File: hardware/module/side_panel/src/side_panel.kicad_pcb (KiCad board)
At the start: 2 copper layers, 96 x 120.2 mm, 35 parts, among them J1 Top Connector, J2 Bottom Connecor, J3 Conn_01x05, J4 Conn_01x09, M1 GA12-N20 12V 60rpm, Q1 AP2302B, U1 ITR8307, U2 ITR8307, U3 ITR8307, U4 PY32F003F1xPx, U5 L9110S, U6 74LVC1G66, U7 NUP4202

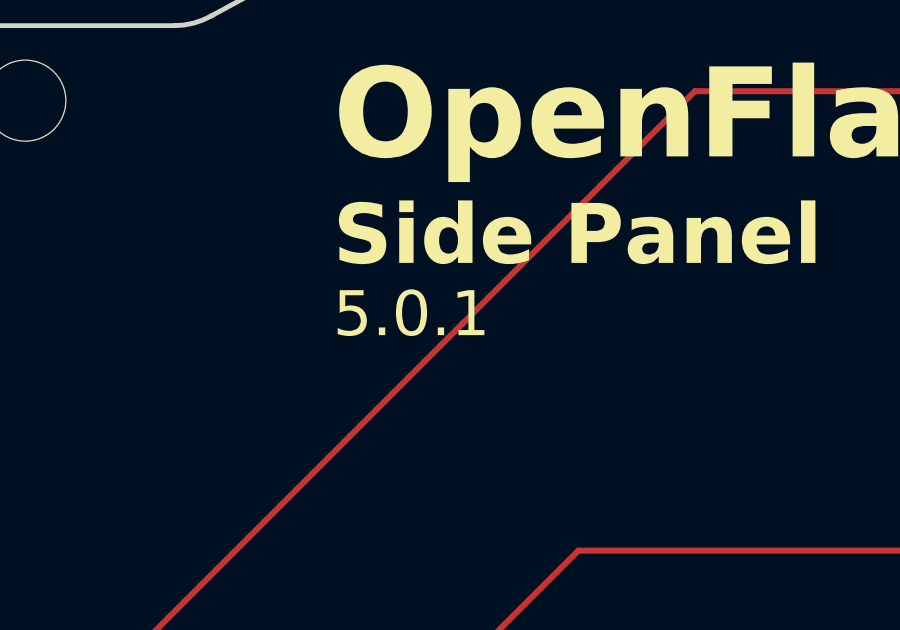
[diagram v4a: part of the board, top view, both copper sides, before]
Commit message: Change sidepanel IR resistor to 15ohm and finalize encoder wheel design
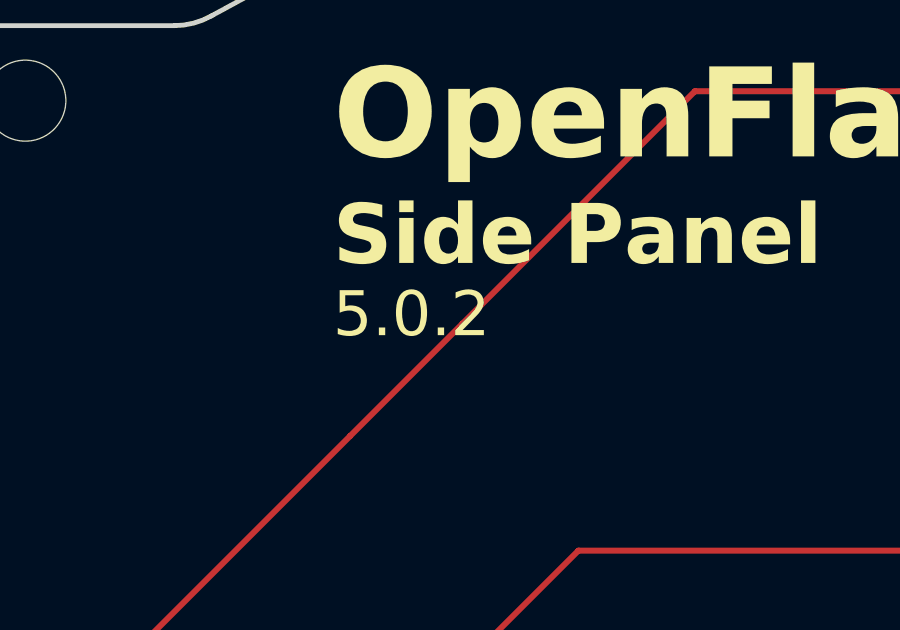
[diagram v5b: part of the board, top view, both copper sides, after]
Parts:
- R4: value 20R -> 15R
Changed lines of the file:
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@@
 		(title "Side Panel")
 		(date "${DATE}")
-		(rev "5.0.1")
+		(rev "5.0.2")
 		(company "OpenFlap")
 		(comment 1 "${GIT_TAG}")
@@
 			)
 		)
-		(property "Value" "20R"
+		(property "Value" "15R"
 			(at 0 1.65 90)
 			(layer "F.Fab")
@@
 			(justify left bottom mirror)
 		)
-		(render_cache "5.0.1" 0
+		(render_cache "5.0.2" 0
 			(polygon
 				(pts
@@
 			(polygon
 				(pts
-					(xy 97.065369 96.427204) (xy 97.065369 96.294213) (xy 96.692043 96.294213) (xy 96.692043 95.11452)
-					(xy 97.065369 95.279384) (xy 97.065369 95.139799) (xy 96.634891 94.950023) (xy 96.540002 94.950023)
-					(xy 96.540002 96.294213) (xy 96.113554 96.294213) (xy 96.113554 96.427204)
+					(xy 97.086618 96.427204) (xy 97.086618 96.315462) (xy 96.495672 95.669562) (xy 96.444194 95.610907)
+					(xy 96.397418 95.550591) (xy 96.387228 95.535839) (xy 96.348943 95.469377) (xy 96.332274 95.427029)
+					(xy 96.317728 95.354394) (xy 96.316154 95.319318) (xy 96.328467 95.240973) (xy 96.365407 95.173551)
+					(xy 96.403715 95.13467) (xy 96.469541 95.093162) (xy 96.546623 95.068884) (xy 96.626464 95.061764)
+					(xy 96.70189 95.067431) (xy 96.773193 95.084433) (xy 96.818439 95.102064) (xy 96.887922 95.14036)
+					(xy 96.95039 95.185025) (xy 97.01016 95.235135) (xy 97.017009 95.241282) (xy 97.105669 95.135769)
+					(xy 97.047485 95.086379) (xy 96.981756 95.038861) (xy 96.915736 94.999864) (xy 96.871562 94.978599)
+					(xy 96.796565 94.951358) (xy 96.719492 94.934206) (xy 96.640345 94.927144) (xy 96.624266 94.926942)
+					(xy 96.544045 94.931772) (xy 96.46962 94.946262) (xy 96.394447 94.973358) (xy 96.387961 94.976401)
+					(xy 96.32217 95.01482) (xy 96.262347 95.066804) (xy 96.225662 95.112688) (xy 96.189495 95.18109)
+					(xy 96.17002 95.256601) (xy 96.166311 95.310892) (xy 96.171687 95.386214) (xy 96.185362 95.447179)
+					(xy 96.213979 95.515446) (xy 96.253139 95.579803) (xy 96.299446 95.64197) (xy 96.349584 95.70194)
+					(xy 96.392357 95.749796) (xy 96.896475 96.296411) (xy 96.134803 96.294213) (xy 96.134803 96.427204)
 				)
 			)
@@
 			(justify left bottom)
 		)
-		(render_cache "5.0.1" 0
+		(render_cache "5.0.2" 0
 			(polygon
 				(pts
@@
 			(polygon
 				(pts
-					(xy 78.91563 96.427204) (xy 78.91563 96.294213) (xy 79.288956 96.294213) (xy 79.288956 95.11452)
-					(xy 78.91563 95.279384) (xy 78.91563 95.139799) (xy 79.346108 94.950023) (xy 79.440997 94.950023)
-					(xy 79.440997 96.294213) (xy 79.867445 96.294213) (xy 79.867445 96.427204)
+					(xy 78.894381 96.427204) (xy 78.894381 96.315462) (xy 79.485327 95.669562) (xy 79.536805 95.610907)
+					(xy 79.583581 95.550591) (xy 79.593771 95.535839) (xy 79.632056 95.469377) (xy 79.648725 95.427029)
+					(xy 79.663271 95.354394) (xy 79.664845 95.319318) (xy 79.652532 95.240973) (xy 79.615592 95.173551)
+					(xy 79.577284 95.13467) (xy 79.511458 95.093162) (xy 79.434376 95.068884) (xy 79.354535 95.061764)
+					(xy 79.279109 95.067431) (xy 79.207806 95.084433) (xy 79.16256 95.102064) (xy 79.093077 95.14036)
+					(xy 79.030609 95.185025) (xy 78.970839 95.235135) (xy 78.96399 95.241282) (xy 78.87533 95.135769)
+					(xy 78.933514 95.086379) (xy 78.999243 95.038861) (xy 79.065263 94.999864) (xy 79.109437 94.978599)
+					(xy 79.184434 94.951358) (xy 79.261507 94.934206) (xy 79.340654 94.927144) (xy 79.356733 94.926942)
+					(xy 79.436954 94.931772) (xy 79.511379 94.946262) (xy 79.586552 94.973358) (xy 79.593038 94.976401)
+					(xy 79.658829 95.01482) (xy 79.718652 95.066804) (xy 79.755337 95.112688) (xy 79.791504 95.18109)
+					(xy 79.810979 95.256601) (xy 79.814688 95.310892) (xy 79.809312 95.386214) (xy 79.795637 95.447179)
+					(xy 79.76702 95.515446) (xy 79.72786 95.579803) (xy 79.681553 95.64197) (xy 79.631415 95.70194)
+					(xy 79.588642 95.749796) (xy 79.084524 96.296411) (xy 79.846196 96.294213) (xy 79.846196 96.427204)
 				)
 			)

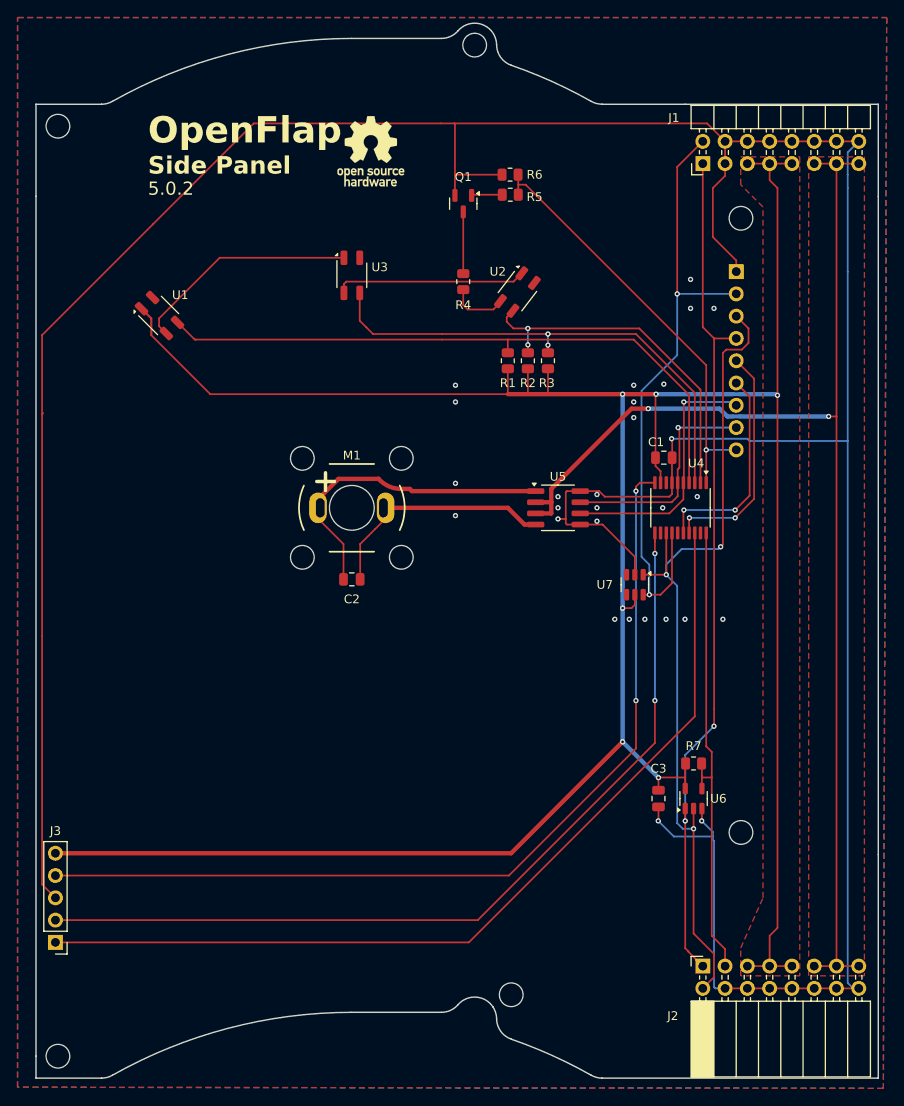
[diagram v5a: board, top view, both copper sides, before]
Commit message: Change CAD design to work with 35mm stepper motor
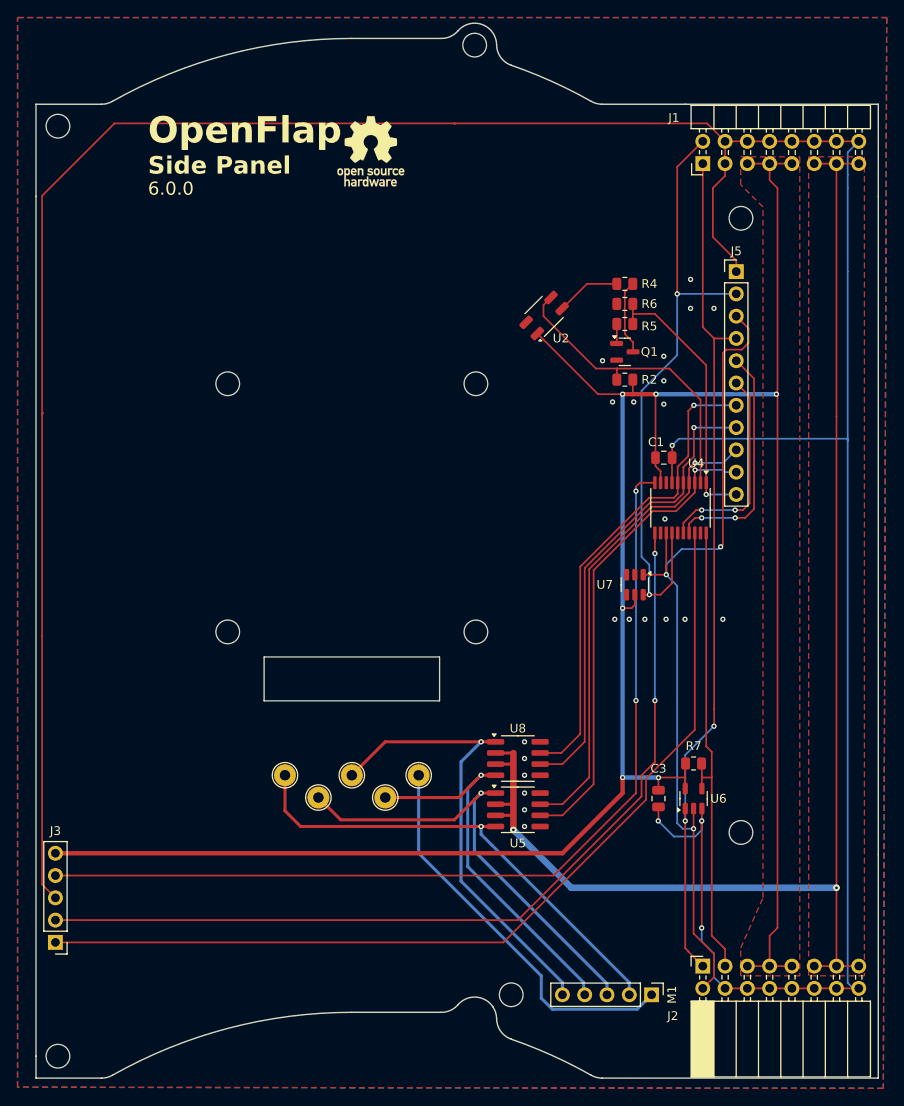
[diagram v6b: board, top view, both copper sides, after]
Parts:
- removed C2: 100nF, Capacitor_SMD:C_0805_2012Metric
- removed J4: Conn_01x09, Connector_PinHeader_2.54mm:PinHeader_1x09_P2.54mm_Vertical
- removed R1, R3: 20K, Resistor_SMD:R_0805_2012Metric
- removed U1, U3: ITR8307, OptoDevice:OnSemi_CASE100CY
- added J5: Conn_01x11, Connector_PinHeader_2.54mm:PinHeader_1x11_P2.54mm_Vertical, F.Cu at (140.8, 105.3)
- added TP1: TestPoint, TestPoint:TestPoint_THTPad_D2.5mm_Drill1.2mm, F.Cu at (93.1, 165.2)
- added TP2: TestPoint, TestPoint:TestPoint_THTPad_D2.5mm_Drill1.2mm, F.Cu at (89.3, 162.7)
- added TP3: TestPoint, TestPoint:TestPoint_THTPad_D2.5mm_Drill1.2mm, F.Cu at (96.9, 162.7)
- added TP4: TestPoint, TestPoint:TestPoint_THTPad_D2.5mm_Drill1.2mm, F.Cu at (100.8, 165.2)
- added TP5: TestPoint, TestPoint:TestPoint_THTPad_D2.5mm_Drill1.2mm, F.Cu at (104.6, 162.7)
- added U8: L9110S, Package_SO:SOP-8_3.76x4.96mm_P1.27mm, F.Cu at (115.9, 160.8)
- M1: value GA12-N20 12V 60rpm -> ~; footprint GA12-N20:GA12-N20 Motor Vertical -> Connector_PinHeader_2.54mm:PinHeader_1x05_P2.54mm_Vertical
- R4: value 15R -> 47R
- moved M1 65.2 mm to (131.1, 187.7), turned to -90 degrees
- moved U5 34.7 mm to (115.9, 166.6)
- moved Q1 25.0 mm to (128.1, 114.4), turned to 0 degrees
- moved R6 19.7 mm to (128.1, 108.9)
- moved R5 19.7 mm to (128.1, 111.2)
- moved R4 18.4 mm to (128.1, 106.7), turned to 0 degrees
- moved H9 12.0 mm to (82.8, 146.3)
- moved H10 12.0 mm to (82.8, 118.0)
- moved H7 12.0 mm to (111.1, 146.3)
- moved H8 12.0 mm to (111.1, 118.0)
- moved R2 11.3 mm to (128.1, 117.6), turned to 180 degrees
- moved U2 4.05 mm to (118.9, 110.3), turned to 135 degrees
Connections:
- net Net-(M1--) renamed /Motor O2
- M1 pad 1: Net-(M1-+) -> /Motor C
- R2 pad 2: /IR Sens B -> /IR Sens A
- U2 pad 1: Net-(U2-A) -> +5V
- U2 pad 3: /IR Sens B -> /IR Sens A
- U4 pad 2: /IR Sens B -> /IR Sens A
- U4 pad 3: /IR Sens Z -> /Motor A1
- U4 pad 4: /IR Sens A -> /Motor A2
- U4 pad 5: /Motor IN_A -> /Motor A3
- U4 pad 6: /Motor IN_B -> /Motor A4
- U5 pad 1: Net-(M1-+) -> /Motor O1
- U5 pad 6: /Motor IN_A -> /Motor A1
- U5 pad 7: /Motor IN_B -> /Motor A2
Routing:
- net /IR Sens Z: track 57.1 -> 0.00 mm, vias 2 -> 0
- net /Motor A4: track 0.00 -> 55.3 mm, vias 0 -> 1
- net /Motor A2: track 0.00 -> 54.6 mm, vias 0 -> 1
- net /Motor A1: track 0.00 -> 54.5 mm, vias 0 -> 1
- net /Motor A3: track 0.00 -> 53.5 mm, vias 0 -> 1
- net +5V: track 324.7 -> 271.7 mm
- net /Motor O3: track 0.00 -> 52.5 mm, vias 0 -> 1
- net /Motor O1: track 0.00 -> 52.1 mm, vias 0 -> 1
- net /Motor C: track 0.00 -> 45.0 mm
- net /Motor O4: track 0.00 -> 44.8 mm, vias 0 -> 1
- net /IR Sens B: track 40.2 -> 0.00 mm, vias 2 -> 0
- net /IR Sens A: track 73.2 -> 35.1 mm
- net GND: track 397.8 -> 362.9 mm, vias 28 -> 26
- net Net-(M1-+): track 34.7 -> 0.00 mm
- net /Motor IN_A: track 29.7 -> 0.00 mm, vias 1 -> 0
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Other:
- outline, holes or cut-outs redrawn
- board text added: "A1"
- board text added: "A2"
- board text added: "A3"
- board text added: "A4"
- board text added: "C"
- board text added: "MOT A1"
- board text added: "MOT A2"
- board text added: "MOT A3"
- board text added: "MOT A4"
- board text removed: "MOT A"
- board text removed: "MOT B"

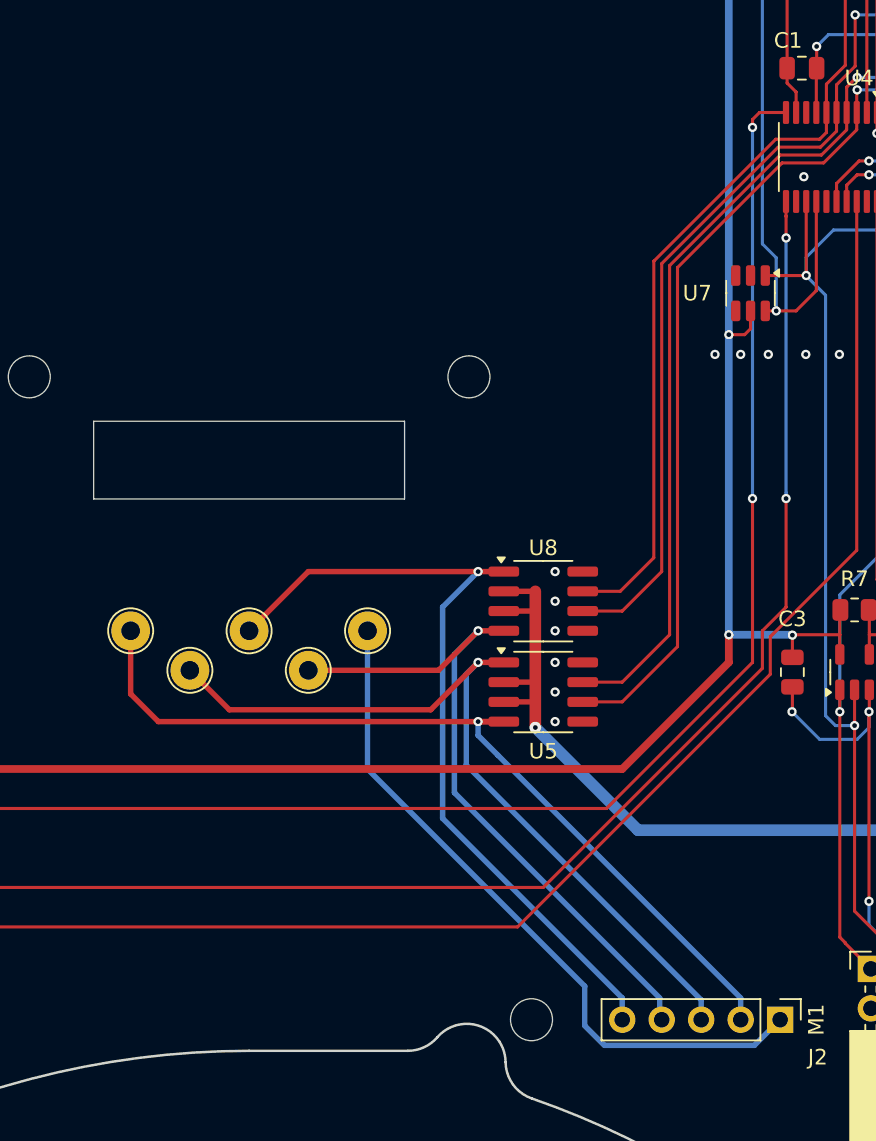
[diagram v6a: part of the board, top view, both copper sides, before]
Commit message: Create proper stepper driver.
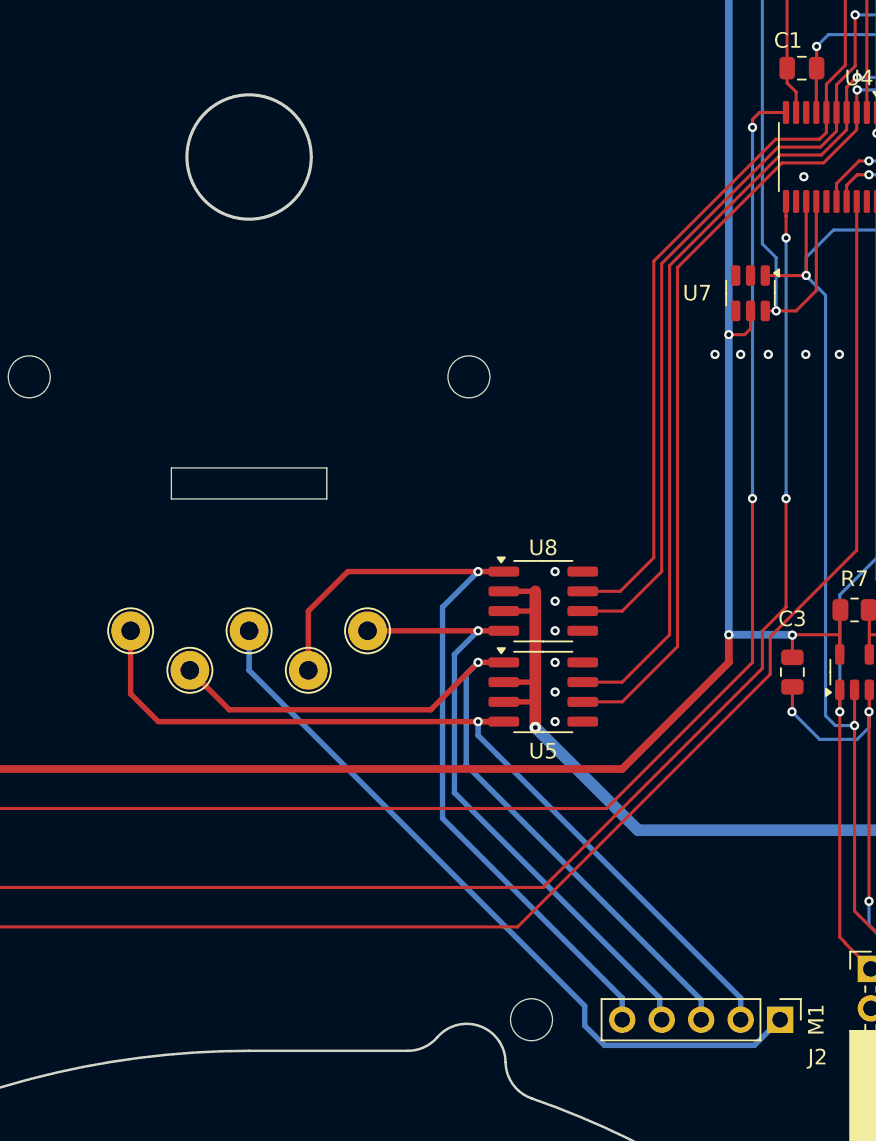
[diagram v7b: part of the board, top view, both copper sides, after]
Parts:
- moved TP5 7.62 mm to (96.9, 162.7)
- moved TP3 4.58 mm to (100.8, 165.2)
- moved TP4 4.58 mm to (104.6, 162.7)
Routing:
- net /Motor O4: track 44.8 -> 39.9 mm
- net /Motor C: track 45.0 -> 48.1 mm
- net /Motor O3: track 52.5 -> 52.0 mm
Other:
- outline, holes or cut-outs redrawn
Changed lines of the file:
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@@
 	(footprint "TestPoint:TestPoint_THTPad_D2.5mm_Drill1.2mm"
 		(layer "F.Cu")
-		(at 104.564 162.662204 90)
+		(at 96.944 162.662204 90)
 		(descr "THT pad as test Point, diameter 2.5mm, hole diameter 1.2mm ")
 		(tags "test point THT pad")
@@
 	(footprint "TestPoint:TestPoint_THTPad_D2.5mm_Drill1.2mm"
 		(layer "F.Cu")
-		(at 100.754 165.202204 90)
+		(at 104.564 162.662204 90)
 		(descr "THT pad as test Point, diameter 2.5mm, hole diameter 1.2mm ")
 		(tags "test point THT pad")
@@
 	(footprint "TestPoint:TestPoint_THTPad_D2.5mm_Drill1.2mm"
 		(layer "F.Cu")
-		(at 96.944 162.662204 90)
+		(at 100.754 165.202204 90)
 		(descr "THT pad as test Point, diameter 2.5mm, hole diameter 1.2mm ")
 		(tags "test point THT pad")
@@
 	)
 	(gr_line
-		(start 106.944 149.182204)
-		(end 106.944 154.182204)
+		(start 101.944 152.182204)
+		(end 101.944 154.182204)
 		(stroke
 			(width 0.05)
@@
 	)
 	(gr_line
-		(start 86.944 149.182204)
-		(end 106.944 149.182204)
+		(start 91.944 154.182204)
+		(end 101.944 154.182204)
 		(stroke
 			(width 0.05)
@@
 		(layer "Edge.Cuts")
 	)
+	(gr_circle
+		(center 96.944 132.182204)
+		(end 100.944 132.182204)
+		(stroke
+			(width 0.2)
+			(type default)
+		)
+		(fill none)
+		(layer "Edge.Cuts")
+	)
 	(gr_line
 		(start 156.947732 197.182204)
@@
 	)
 	(gr_line
-		(start 106.944 154.182204)
-		(end 86.944 154.182204)
+		(start 91.944 152.182204)
+		(end 101.944 152.182204)
 		(stroke
 			(width 0.05)
@@
 	)
 	(gr_line
-		(start 86.944 154.182204)
-		(end 86.944 149.182204)
+		(start 91.944 154.182204)
+		(end 91.944 152.182204)
 		(stroke
 			(width 0.05)
@@
 	(segment
 		(start 111.676 162.662204)
-		(end 109.136 165.202204)
-		(width 0.35)
-		(layer "F.Cu")
-		(net 25)
-	)
-	(segment
-		(start 109.136 165.202204)
-		(end 100.754 165.202204)
+		(end 104.564 162.662204)
 		(width 0.35)
 		(layer "F.Cu")
@@
 	)
 	(segment
-		(start 113.3295 158.852204)
-		(end 111.676 158.852204)
+		(start 100.754 161.392204)
+		(end 100.754 165.202204)
 		(width 0.35)
 		(layer "F.Cu")
@@
 	)
 	(segment
-		(start 111.676 158.852204)
-		(end 100.754 158.852204)
+		(start 103.294 158.852204)
+		(end 100.754 161.392204)
 		(width 0.35)
 		(layer "F.Cu")
@@
 	)
 	(segment
-		(start 100.754 158.852204)
-		(end 96.944 162.662204)
+		(start 113.3295 158.852204)
+		(end 111.676 158.852204)
+		(width 0.35)
+		(layer "F.Cu")
+		(net 27)
+	)
+	(segment
+		(start 111.676 158.852204)
+		(end 103.294 158.852204)
 		(width 0.35)
 		(layer "F.Cu")
@@
 	)
 	(segment
-		(start 129.456 189.332204)
-		(end 131.107 187.681204)
+		(start 119.804 189.332204)
+		(end 118.534 188.062204)
 		(width 0.35)
 		(layer "B.Cu")
@@
 	)
 	(segment
-		(start 104.564 171.552204)
-		(end 118.534 185.522204)
+		(start 96.944 165.202204)
+		(end 96.944 162.662204)
 		(width 0.35)
 		(layer "B.Cu")
@@
 	)
 	(segment
-		(start 104.564 162.662204)
-		(end 104.564 171.552204)
+		(start 131.107 187.681204)
+		(end 129.456 189.332204)
 		(width 0.35)
 		(layer "B.Cu")
@@
 	)
 	(segment
-		(start 118.534 188.062204)
-		(end 119.804 189.332204)
+		(start 118.534 186.792204)
+		(end 96.944 165.202204)
 		(width 0.35)
 		(layer "B.Cu")
@@
 	)
 	(segment
-		(start 118.534 185.522204)
-		(end 118.534 188.062204)
+		(start 129.456 189.332204)
+		(end 119.804 189.332204)
 		(width 0.35)
 		(layer "B.Cu")
@@
 	)
 	(segment
-		(start 119.804 189.332204)
-		(end 129.456 189.332204)
+		(start 118.534 188.062204)
+		(end 118.534 186.792204)
 		(width 0.35)
 		(layer "B.Cu")
